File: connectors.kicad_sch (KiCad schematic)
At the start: 4 parts, among them J1 Conn_01x04_Pin, J2 Conn_01x09_Pin, J3 Conn_01x04_Pin, J4 Conn_02x03_Odd_Even

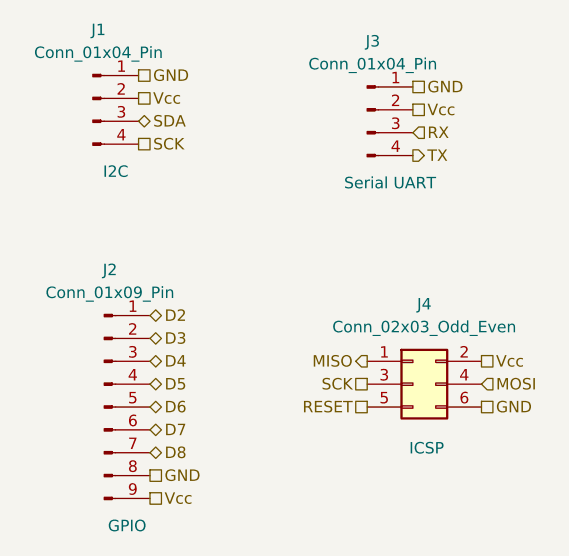
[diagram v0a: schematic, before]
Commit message: Fixed Bugs at 4layer
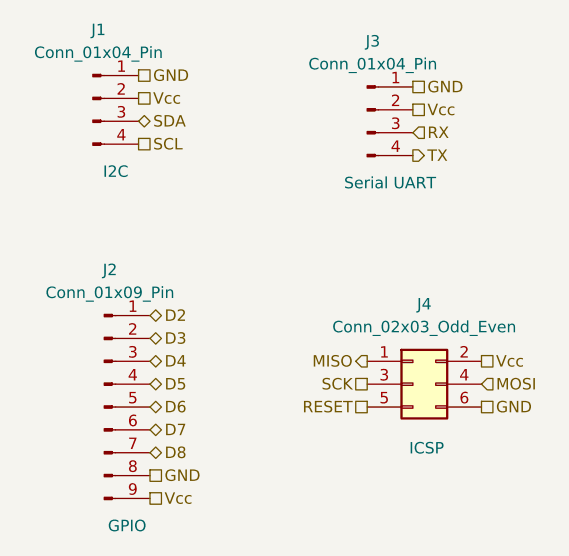
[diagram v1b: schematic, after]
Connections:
- net SCK: no longer J1.4 (Pin_4)
- new net SCL: J1.4 (Pin_4)
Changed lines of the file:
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@@
 		)
 	)
-	(hierarchical_label "SCK"
+	(hierarchical_label "SCL"
 		(shape passive)
 		(at 97.79 60.96 0)
